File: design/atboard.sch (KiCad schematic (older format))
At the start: 5 parts, among them J1 AVR_SPI, U1 ATmega328-PU, Y1 8 MHz

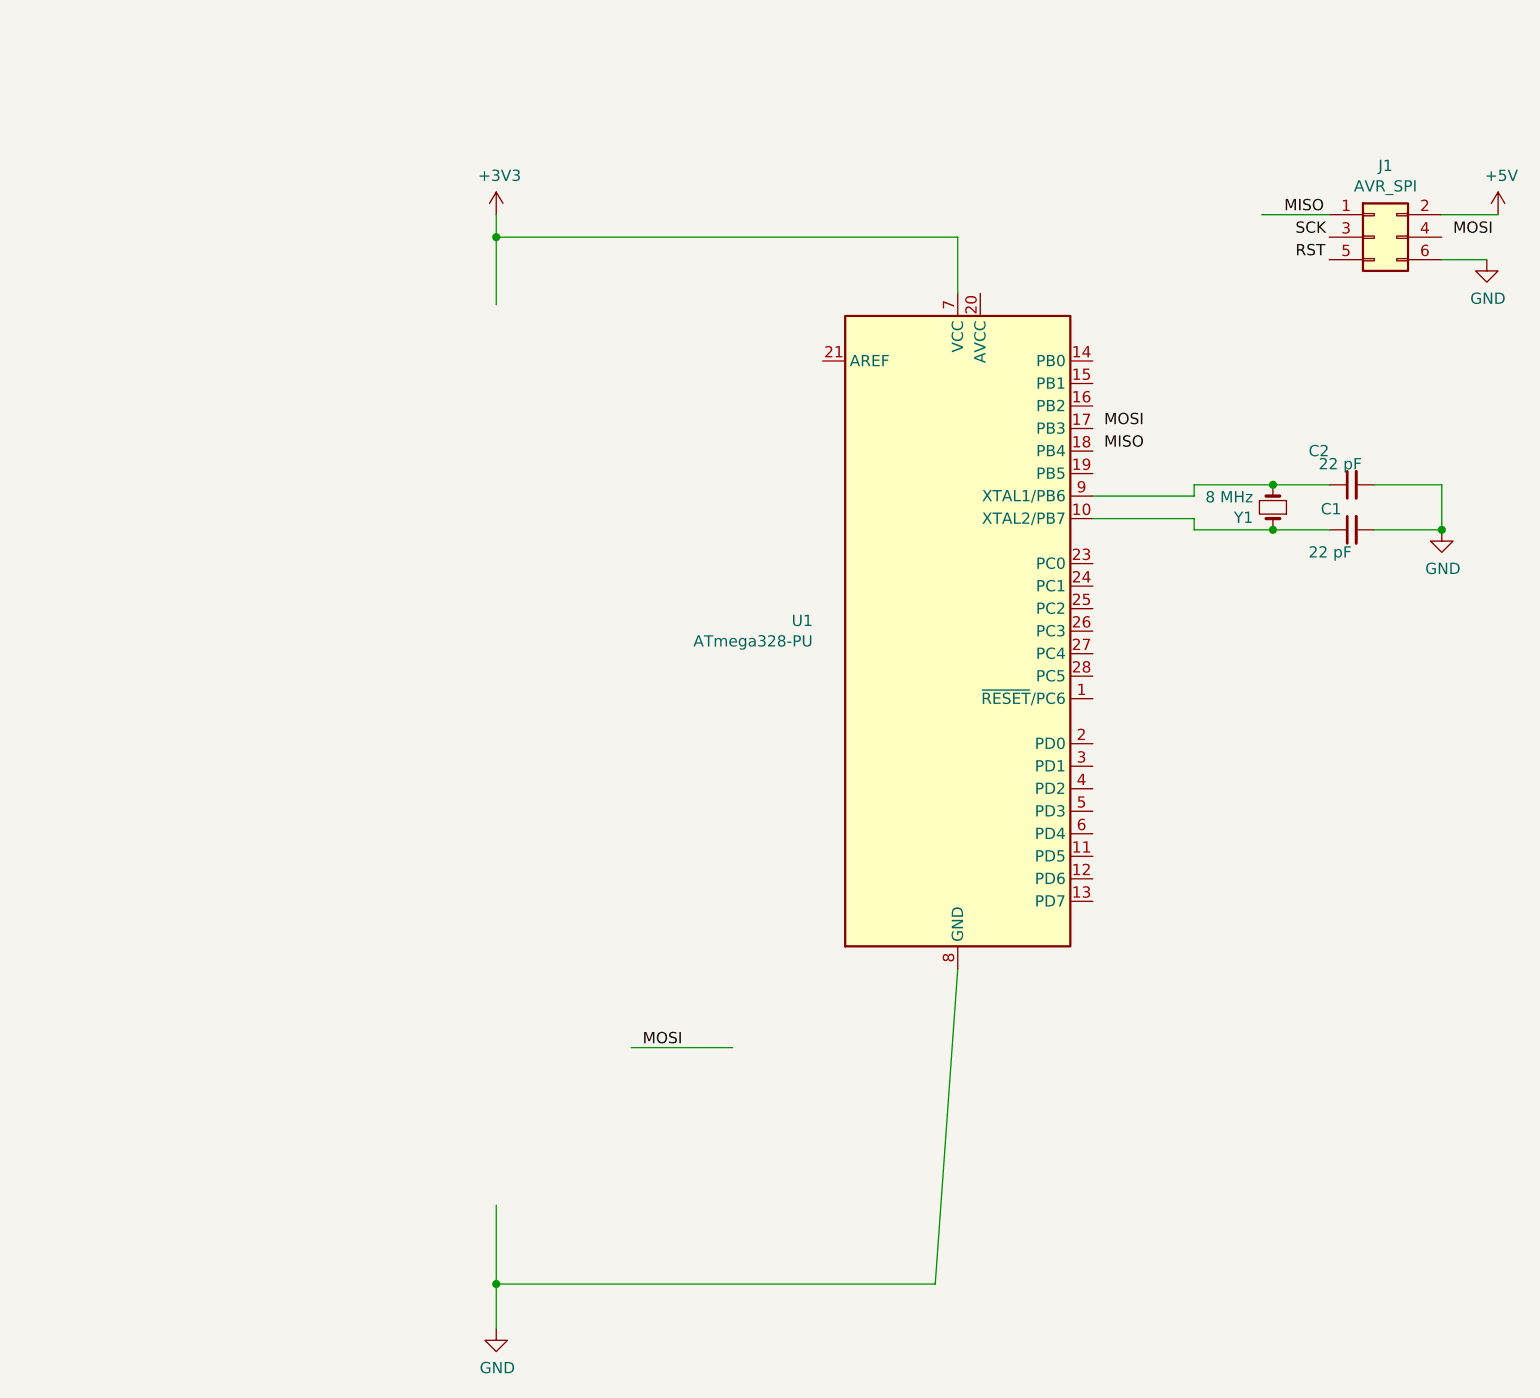
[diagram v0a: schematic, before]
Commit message: progressing on pcb design
still need connector for RAW, VCC and GND
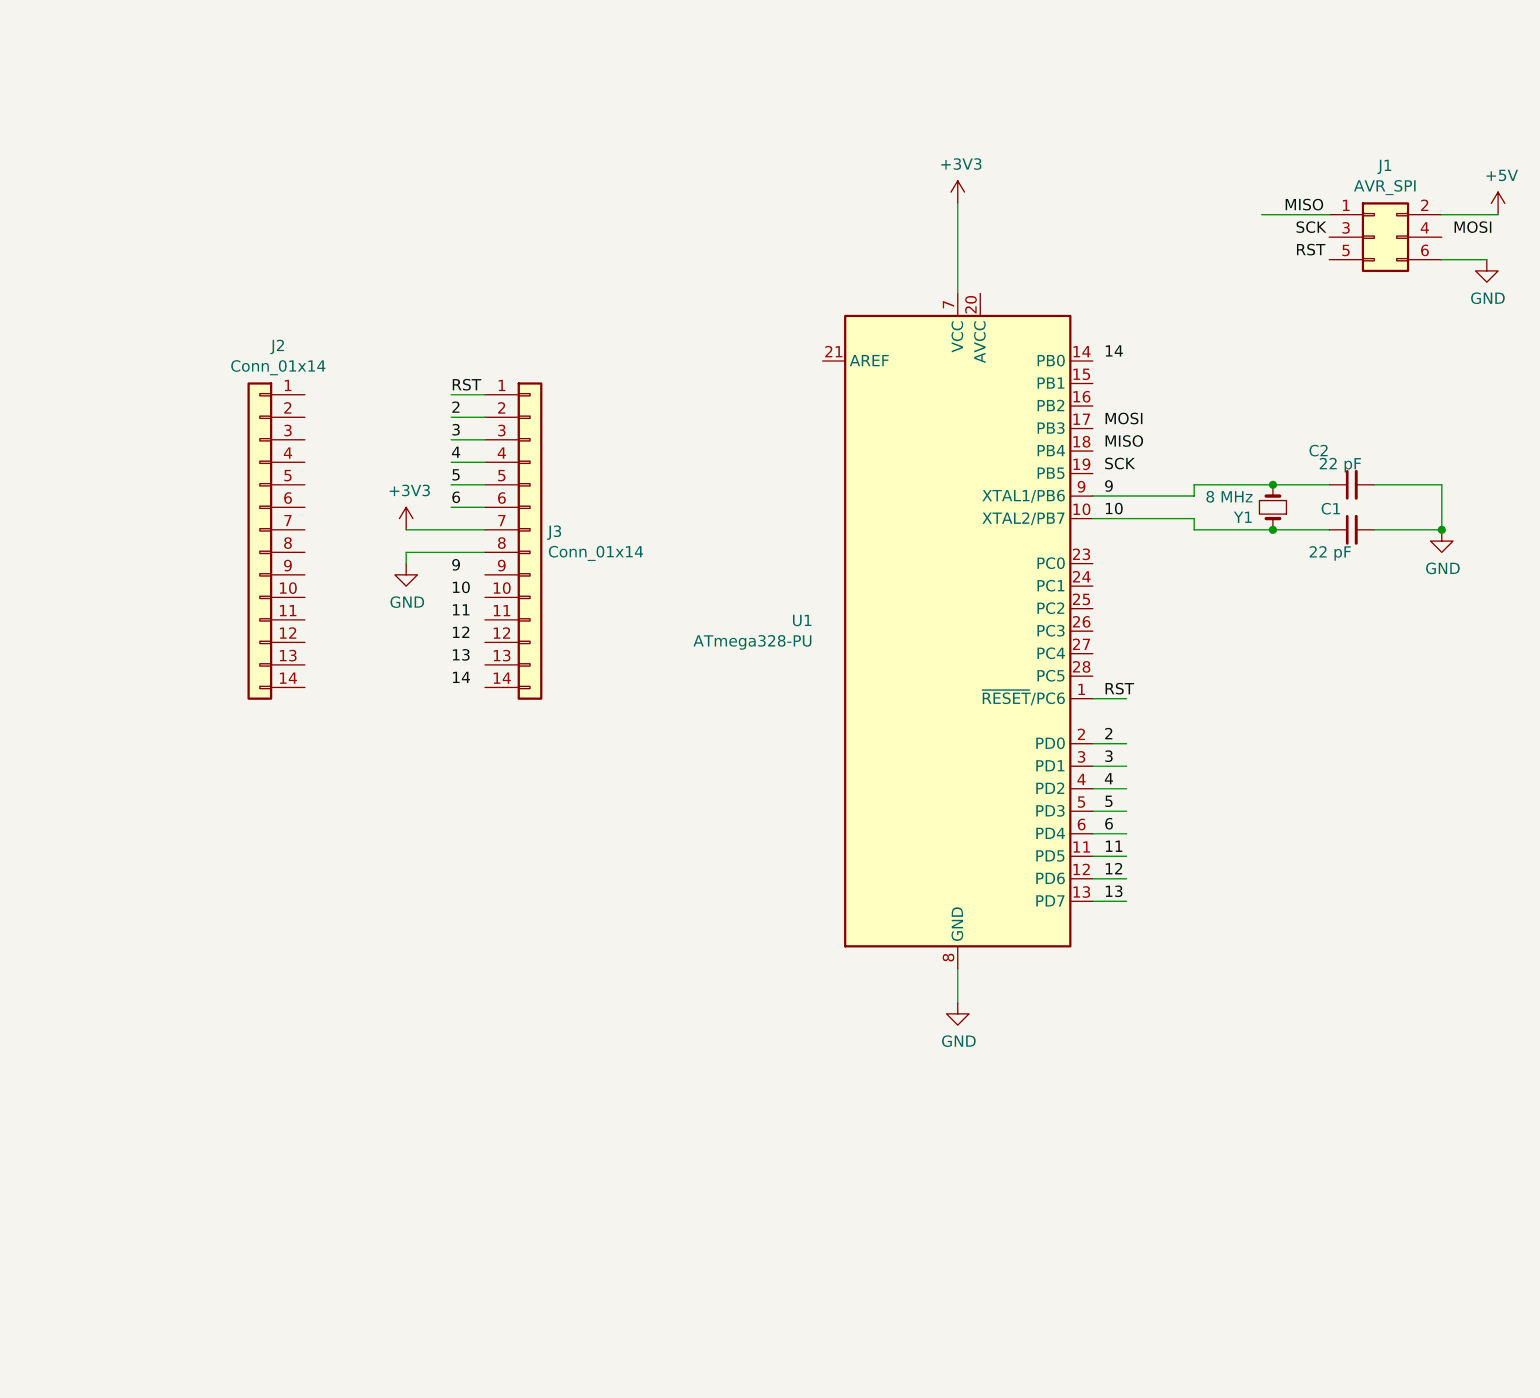
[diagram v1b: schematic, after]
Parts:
- added J2, J3: Conn_01x14, Connector_PinHeader_2.54mm:PinHeader_1x14_P2.54mm_Vertical, symbol Connector_Generic:Conn_01x14
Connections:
- net labels added: 10, 11, 12, 13, 14, 2, 3, 4, 5, 6, 9
- wire segments 23 -> 34
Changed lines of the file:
@@
 L power:+3V3 #PWR0101
 U 1 1 5CBE8F4B
-P 4300 2350
-F 0 "#PWR0101" H 4300 2200 50  0001 C CNN
-F 1 "+3V3" H 4315 2523 50  0000 C CNN
-F 2 "" H 4300 2350 50  0001 C CNN
-F 3 "" H 4300 2350 50  0001 C CNN
-	1    4300 2350
-	1    0    0    -1
-$EndComp
-Wire Wire Line
-	4300 2350 4300 2450
+P 6350 2300
+F 0 "#PWR0101" H 6350 2150 50  0001 C CNN
+F 1 "+3V3" H 6365 2473 50  0000 C CNN
+F 2 "" H 6350 2300 50  0001 C CNN
+F 3 "" H 6350 2300 50  0001 C CNN
+	1    6350 2300
+	1    0    0    -1
+$EndComp
 $Comp
 L power:GND #PWR0102
 U 1 1 5CBE9BF8
-P 4300 7300
-F 0 "#PWR0102" H 4300 7050 50  0001 C CNN
-F 1 "GND" H 4305 7127 50  0000 C CNN
-F 2 "" H 4300 7300 50  0001 C CNN
-F 3 "" H 4300 7300 50  0001 C CNN
-	1    4300 7300
-	1    0    0    -1
-$EndComp
-Wire Wire Line
-	4300 6750 4300 7100
+P 6350 5850
+F 0 "#PWR0102" H 6350 5600 50  0001 C CNN
+F 1 "GND" H 6355 5677 50  0000 C CNN
+F 2 "" H 6350 5850 50  0001 C CNN
+F 3 "" H 6350 5850 50  0001 C CNN
+	1    6350 5850
+	1    0    0    -1
+$EndComp
 $Comp
 L Device:C_Small C2
@@
 Text Label 7800 2350 0    50   ~ 0
 MISO
-Text Label 4950 6050 0    50   ~ 0
-MOSI
-Wire Wire Line
-	4900 6050 5350 6050
 Wire Wire Line
 	8000 2350 7700 2350
@@
 Wire Wire Line
 	8700 2550 8500 2550
-Wire Wire Line
-	6350 5700 6250 7100
-Wire Wire Line
-	6250 7100 4300 7100
-Connection ~ 4300 7100
-Wire Wire Line
-	4300 7100 4300 7300
 $Comp
 L MCU_Microchip_ATmega:ATmega328-PU U1
@@
 	1    0    0    -1
 $EndComp
-Wire Wire Line
-	6350 2700 6350 2450
-Wire Wire Line
-	6350 2450 4300 2450
-Connection ~ 4300 2450
-Wire Wire Line
-	4300 2450 4300 2750
 Wire Wire Line
 	8000 3550 7750 3550
@@
 RST
 $Comp
-L power:+5V #PWR?
+L power:+5V #PWR0105
 U 1 1 5CC03FF7
 P 8750 2350
-F 0 "#PWR?" H 8750 2200 50  0001 C CNN
+F 0 "#PWR0105" H 8750 2200 50  0001 C CNN
 F 1 "+5V" H 8765 2523 50  0000 C CNN
 F 2 "" H 8750 2350 50  0001 C CNN
@@
 Wire Wire Line
 	8750 2350 8500 2350
+Text Label 7000 3500 0    50   ~ 0
+SCK
+Text Label 7000 4500 0    50   ~ 0
+RST
+$Comp
+L Connector_Generic:Conn_01x14 J3
+U 1 1 5CC092D8
+P 4450 3750
+F 0 "J3" H 4530 3742 50  0000 L CNN
+F 1 "Conn_01x14" H 4530 3651 50  0000 L CNN
+F 2 "Connector_PinHeader_2.54mm:PinHeader_1x14_P2.54mm_Vertical" H 4450 3750 50  0001 C CNN
+F 3 "~" H 4450 3750 50  0001 C CNN
+	1    4450 3750
+	1    0    0    -1
+$EndComp
+$Comp
+L Connector_Generic:Conn_01x14 J2
+U 1 1 5CC0C46F
+P 3250 3750
+F 0 "J2" H 3168 4567 50  0000 C CNN
+F 1 "Conn_01x14" H 3168 4476 50  0000 C CNN
+F 2 "Connector_PinHeader_2.54mm:PinHeader_1x14_P2.54mm_Vertical" H 3250 3750 50  0001 C CNN
+F 3 "~" H 3250 3750 50  0001 C CNN
+	1    3250 3750
+	-1   0    0    -1
+$EndComp
+Text Label 4100 3150 0    50   ~ 0
+RST
+Text Label 4100 3250 0    50   ~ 0
+2
+Text Label 4100 3350 0    50   ~ 0
+3
+Text Label 4100 3450 0    50   ~ 0
+4
+Text Label 4100 3550 0    50   ~ 0
+5
+Text Label 4100 3650 0    50   ~ 0
+6
+$Comp
+L power:+3V3 #PWR0106
+U 1 1 5CC0EBC6
+P 3900 3750
+F 0 "#PWR0106" H 3900 3600 50  0001 C CNN
+F 1 "+3V3" H 3915 3923 50  0000 C CNN
+F 2 "" H 3900 3750 50  0001 C CNN
+F 3 "" H 3900 3750 50  0001 C CNN
+	1    3900 3750
+	1    0    0    -1
+$EndComp
+Wire Wire Line
+	4250 3750 3900 3750
+Wire Wire Line
+	4250 3150 4100 3150
+Wire Wire Line
+	4250 3250 4100 3250
+Wire Wire Line
+	4250 3350 4100 3350
+Wire Wire Line
+	4250 3450 4100 3450
+Wire Wire Line
+	4250 3550 4100 3550
+Wire Wire Line
+	4250 3650 4100 3650
+$Comp
+L power:GND #PWR0107
+U 1 1 5CC12E7E
+P 3900 3900
+F 0 "#PWR0107" H 3900 3650 50  0001 C CNN
+F 1 "GND" H 3905 3727 50  0000 C CNN
+F 2 "" H 3900 3900 50  0001 C CNN
+F 3 "" H 3900 3900 50  0001 C CNN
+	1    3900 3900
+	1    0    0    -1
+$EndComp
+Wire Wire Line
+	4250 3850 3900 3850
+Wire Wire Line
+	3900 3850 3900 3900
+Text Label 4100 3950 0    50   ~ 0
+9
+Text Label 4100 4050 0    50   ~ 0
+10
+Text Label 4100 4150 0    50   ~ 0
+11
+Text Label 4100 4250 0    50   ~ 0
+12
+Text Label 4100 4350 0    50   ~ 0
+13
+Text Label 4100 4450 0    50   ~ 0
+14
+Text Label 7000 3000 0    50   ~ 0
+14
+Text Label 7000 5400 0    50   ~ 0
+13
+Text Label 7000 5300 0    50   ~ 0
+12
+Text Label 7000 5200 0    50   ~ 0
+11
+Text Label 7000 3700 0    50   ~ 0
+10
+Text Label 7000 3600 0    50   ~ 0
+9
+Wire Wire Line
+	6350 5700 6350 5850
+Wire Wire Line
+	6350 2300 6350 2700
+Text Label 7000 5100 0    50   ~ 0
+6
+Text Label 7000 5000 0    50   ~ 0
+5
+Text Label 7000 4900 0    50   ~ 0
+4
+Text Label 7000 4800 0    50   ~ 0
+3
+Text Label 7000 4700 0    50   ~ 0
+2
+Wire Wire Line
+	6950 5400 7100 5400
+Wire Wire Line
+	6950 5300 7100 5300
+Wire Wire Line
+	6950 5200 7100 5200
+Wire Wire Line
+	6950 5100 7100 5100
+Wire Wire Line
+	6950 5000 7100 5000
+Wire Wire Line
+	6950 4900 7100 4900
+Wire Wire Line
+	6950 4800 7100 4800
+Wire Wire Line
+	6950 4700 7100 4700
+Wire Wire Line
+	6950 4500 7100 4500
 $EndSCHEMATC

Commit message: done for the night
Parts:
- Y1: footprint Crystal:Crystal_HC49-U_Horizontal -> Crystal:Crystal_HC49-4H_Vertical
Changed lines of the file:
@@
 F 0 "Y1" V 7704 3738 50  0000 L CNN
 F 1 "8 MHz" V 7795 3738 50  0000 L CNN
-F 2 "Crystal:Crystal_HC49-U_Horizontal" H 7750 3650 50  0001 C CNN
+F 2 "Crystal:Crystal_HC49-4H_Vertical" H 7750 3650 50  0001 C CNN
 F 3 "~" H 7750 3650 50  0001 C CNN
 	1    7750 3650
